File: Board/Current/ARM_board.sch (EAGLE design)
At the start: 171 parts, among them IC3 STM32F437VI, IC4 LM358DT, J1 USART/I2C, J10 ANALOG, J11 DGND, J12 DPWR, J13 DIGITAL, J14 SGND, J15 SPWR, J16 SERVO, J2 I2C2/USART3, J3 USART2, J5 SPI, J6 Bluesmirf, J7 SWD, J8 AGND, J9 APWR, Q1 STL4P2UH7, Q2 2STR1230, SW1 SW, U1 LSM330DLC, U10 BAV99, U11 BAV99, U12 USBLC6-2, U13 USBLC6-2, U14 STMPS2171MTR, U15 MC74HC164, U3 NC7SZU04, U4 L6206Q, U5 L6206Q, U6 SI7617, U7 SI7617, U8 SI7617, U9 SI7617, Y2 8MHz

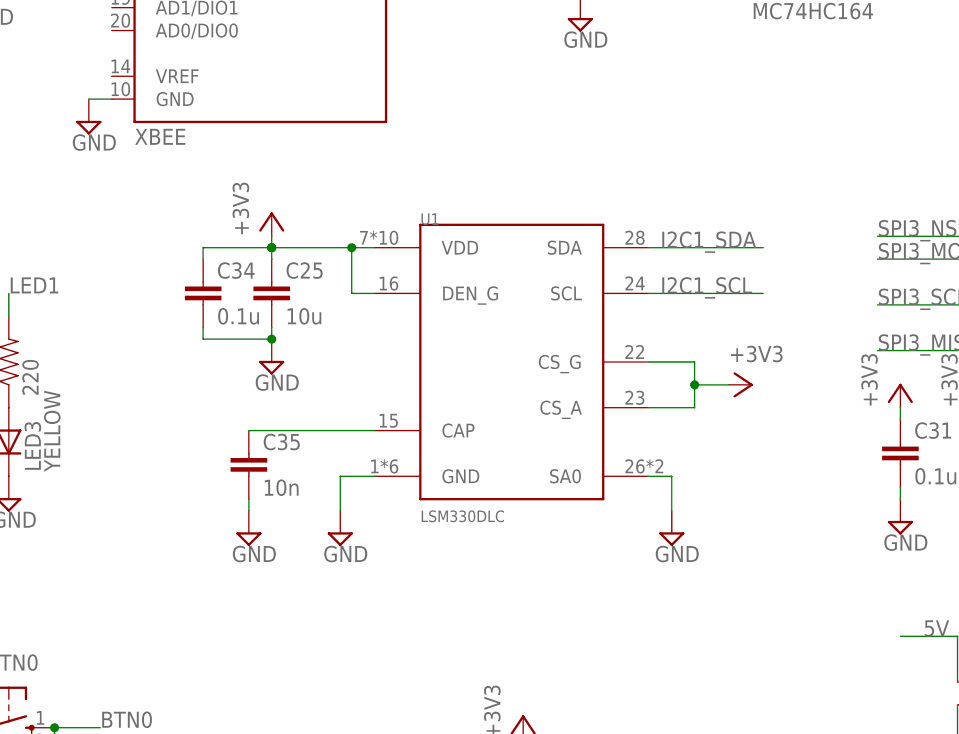
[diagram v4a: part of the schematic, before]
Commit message: Replaced LSM330DLC with LSM330 and re-added horse
LSM330 replaced LSM330DLC.
Re-added horse logo to board.
Moved labels in UART1 box down slightly.
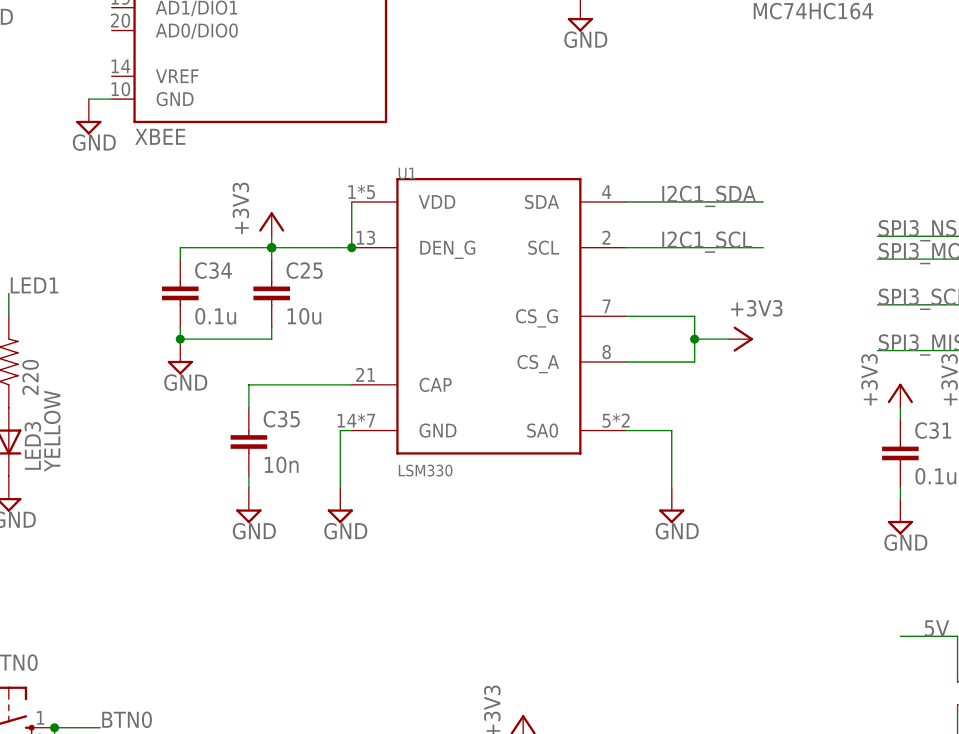
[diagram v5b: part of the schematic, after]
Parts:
- U1: value LSM330DLC -> LSM330; device r_cubed:LSM330DLC -> r_cubed:LSM330
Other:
- moved on the sheet: C34, C35, U1
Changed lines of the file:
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@@
 <setting verticaltext="up"/>
 </settings>
-<grid distance="0.05" unitdist="inch" unit="inch" style="lines" multiple="1" display="no" altdistance="0.01" altunitdist="inch" altunit="inch"/>
+<grid distance="0.1" unitdist="inch" unit="inch" style="lines" multiple="1" display="no" altdistance="0.01" altunitdist="inch" altunit="inch"/>
 <layers>
 <layer number="1" name="Top" color="4" fill="1" visible="no" active="no"/>
@@
 <part name="C43" library="SparkFun" deviceset="CAP" device="0402-CAP" value="0.1u"/>
 <part name="C44" library="SparkFun" deviceset="CAP_POL" device="D" value="680uF"/>
-<part name="U1" library="r_cubed" deviceset="LSM330DLC" device=""/>
+<part name="U1" library="r_cubed" deviceset="LSM330" device=""/>
 <part name="SUPPLY36" library="supply2" deviceset="GND" device=""/>
 <part name="SUPPLY55" library="supply2" deviceset="GND" device=""/>
@@
 <instance part="SUPPLY54" gate="GND" x="27.94" y="278.13"/>
 <instance part="C25" gate="G$1" x="271.78" y="82.55"/>
-<instance part="C34" gate="G$1" x="264.16" y="82.55"/>
-<instance part="C35" gate="G$1" x="269.24" y="63.5"/>
-<instance part="SUPPLY59" gate="GND" x="316.23" y="57.15"/>
-<instance part="SUPPLY61" gate="GND" x="271.78" y="76.2"/>
+<instance part="C34" gate="G$1" x="261.62" y="82.55"/>
+<instance part="C35" gate="G$1" x="269.24" y="66.04"/>
+<instance part="SUPPLY59" gate="GND" x="316.23" y="59.69"/>
+<instance part="SUPPLY61" gate="GND" x="261.62" y="76.2"/>
 <instance part="+3V2" gate="G$1" x="189.23" y="180.34" smashed="yes">
 <attribute name="VALUE" x="186.69" y="177.8" size="1.778" layer="96" rot="R90"/>
@@
 <instance part="C44" gate="G$1" x="228.6" y="237.49"/>
 <instance part="U1" gate="G$1" x="295.91" y="81.28"/>
-<instance part="SUPPLY36" gate="GND" x="279.4" y="57.15"/>
-<instance part="SUPPLY55" gate="GND" x="269.24" y="57.15"/>
-<instance part="+3V8" gate="G$1" x="325.12" y="73.66" smashed="yes" rot="R270">
-<attribute name="VALUE" x="322.58" y="76.2" size="1.778" layer="96"/>
+<instance part="SUPPLY36" gate="GND" x="279.4" y="59.69"/>
+<instance part="SUPPLY55" gate="GND" x="269.24" y="59.69"/>
+<instance part="+3V8" gate="G$1" x="325.12" y="78.74" smashed="yes" rot="R270">
+<attribute name="VALUE" x="322.58" y="81.28" size="1.778" layer="96"/>
 </instance>
 <instance part="U14" gate="G$1" x="304.8" y="222.25"/>
@@
 <pinref part="U1" gate="G$1" pin="GND"/>
 <pinref part="SUPPLY36" gate="GND" pin="GND"/>
-<wire x1="283.21" y1="63.5" x2="279.4" y2="63.5" width="0.1524" layer="91"/>
-<wire x1="279.4" y1="63.5" x2="279.4" y2="59.69" width="0.1524" layer="91"/>
+<wire x1="280.67" y1="68.58" x2="279.4" y2="68.58" width="0.1524" layer="91"/>
+<wire x1="279.4" y1="68.58" x2="279.4" y2="62.23" width="0.1524" layer="91"/>
 </segment>
 <segment>
 <pinref part="C34" gate="G$1" pin="2"/>
-<wire x1="264.16" y1="80.01" x2="264.16" y2="78.74" width="0.1524" layer="91"/>
+<wire x1="261.62" y1="80.01" x2="261.62" y2="78.74" width="0.1524" layer="91"/>
 <pinref part="SUPPLY61" gate="GND" pin="GND"/>
-<wire x1="264.16" y1="78.74" x2="271.78" y2="78.74" width="0.1524" layer="91"/>
 <pinref part="C25" gate="G$1" pin="2"/>
+<wire x1="261.62" y1="78.74" x2="271.78" y2="78.74" width="0.1524" layer="91"/>
 <wire x1="271.78" y1="78.74" x2="271.78" y2="80.01" width="0.1524" layer="91"/>
-<junction x="271.78" y="78.74"/>
+<junction x="261.62" y="78.74"/>
 </segment>
 <segment>
 <pinref part="C35" gate="G$1" pin="2"/>
 <pinref part="SUPPLY55" gate="GND" pin="GND"/>
-<wire x1="269.24" y1="60.96" x2="269.24" y2="59.69" width="0.1524" layer="91"/>
+<wire x1="269.24" y1="63.5" x2="269.24" y2="62.23" width="0.1524" layer="91"/>
 </segment>
 <segment>
 <pinref part="U1" gate="G$1" pin="SA0"/>
 <pinref part="SUPPLY59" gate="GND" pin="GND"/>
-<wire x1="313.69" y1="63.5" x2="316.23" y2="63.5" width="0.1524" layer="91"/>
-<wire x1="316.23" y1="63.5" x2="316.23" y2="59.69" width="0.1524" layer="91"/>
+<wire x1="311.15" y1="68.58" x2="316.23" y2="68.58" width="0.1524" layer="91"/>
+<wire x1="316.23" y1="68.58" x2="316.23" y2="62.23" width="0.1524" layer="91"/>
 </segment>
 <segment>
@@
 <segment>
 <pinref part="U1" gate="G$1" pin="SCL"/>
-<wire x1="313.69" y1="83.82" x2="326.39" y2="83.82" width="0.1524" layer="91"/>
-<label x="314.96" y="83.82" size="1.778" layer="95"/>
+<wire x1="311.15" y1="88.9" x2="326.39" y2="88.9" width="0.1524" layer="91"/>
+<label x="314.96" y="88.9" size="1.778" layer="95"/>
 </segment>
 <segment>
@@
 <segment>
 <pinref part="U1" gate="G$1" pin="SDA"/>
-<wire x1="313.69" y1="88.9" x2="326.39" y2="88.9" width="0.1524" layer="91"/>
-<label x="314.96" y="88.9" size="1.778" layer="95"/>
+<wire x1="311.15" y1="93.98" x2="326.39" y2="93.98" width="0.1524" layer="91"/>
+<label x="314.96" y="93.98" size="1.778" layer="95"/>
 </segment>
 <segment>
@@
 <segment>
 <pinref part="C34" gate="G$1" pin="1"/>
-<wire x1="264.16" y1="87.63" x2="264.16" y2="88.9" width="0.1524" layer="91"/>
+<wire x1="261.62" y1="87.63" x2="261.62" y2="88.9" width="0.1524" layer="91"/>
 <pinref part="+3V28" gate="G$1" pin="+3V3"/>
-<wire x1="264.16" y1="88.9" x2="271.78" y2="88.9" width="0.1524" layer="91"/>
+<wire x1="261.62" y1="88.9" x2="271.78" y2="88.9" width="0.1524" layer="91"/>
 <wire x1="271.78" y1="88.9" x2="271.78" y2="90.17" width="0.1524" layer="91"/>
 <pinref part="C25" gate="G$1" pin="1"/>
@@
 <wire x1="271.78" y1="88.9" x2="280.67" y2="88.9" width="0.1524" layer="91"/>
 <pinref part="U1" gate="G$1" pin="VDD"/>
-<wire x1="280.67" y1="88.9" x2="283.21" y2="88.9" width="0.1524" layer="91"/>
+<wire x1="280.67" y1="88.9" x2="280.67" y2="93.98" width="0.1524" layer="91"/>
 <junction x="271.78" y="88.9"/>
 <pinref part="U1" gate="G$1" pin="DEN_G"/>
-<wire x1="283.21" y1="83.82" x2="280.67" y2="83.82" width="0.1524" layer="91"/>
-<wire x1="280.67" y1="83.82" x2="280.67" y2="88.9" width="0.1524" layer="91"/>
 <junction x="280.67" y="88.9"/>
 </segment>
 <segment>
 <pinref part="U1" gate="G$1" pin="CS_A"/>
-<wire x1="313.69" y1="71.12" x2="318.77" y2="71.12" width="0.1524" layer="91"/>
-<wire x1="318.77" y1="71.12" x2="318.77" y2="73.66" width="0.1524" layer="91"/>
+<wire x1="311.15" y1="76.2" x2="318.77" y2="76.2" width="0.1524" layer="91"/>
+<wire x1="318.77" y1="76.2" x2="318.77" y2="78.74" width="0.1524" layer="91"/>
 <pinref part="U1" gate="G$1" pin="CS_G"/>
-<wire x1="318.77" y1="73.66" x2="318.77" y2="76.2" width="0.1524" layer="91"/>
-<wire x1="318.77" y1="76.2" x2="313.69" y2="76.2" width="0.1524" layer="91"/>
+<wire x1="318.77" y1="78.74" x2="318.77" y2="81.28" width="0.1524" layer="91"/>
+<wire x1="318.77" y1="81.28" x2="311.15" y2="81.28" width="0.1524" layer="91"/>
 <pinref part="+3V8" gate="G$1" pin="+3V3"/>
-<wire x1="322.58" y1="73.66" x2="318.77" y2="73.66" width="0.1524" layer="91"/>
-<junction x="318.77" y="73.66"/>
+<wire x1="322.58" y1="78.74" x2="318.77" y2="78.74" width="0.1524" layer="91"/>
+<junction x="318.77" y="78.74"/>
 </segment>
 <segment>
@@
 <pinref part="C35" gate="G$1" pin="1"/>
 <pinref part="U1" gate="G$1" pin="CAP"/>
-<wire x1="269.24" y1="68.58" x2="283.21" y2="68.58" width="0.1524" layer="91"/>
+<wire x1="269.24" y1="71.12" x2="269.24" y2="73.66" width="0.1524" layer="91"/>
+<wire x1="269.24" y1="73.66" x2="280.67" y2="73.66" width="0.1524" layer="91"/>
 </segment>
 </net>

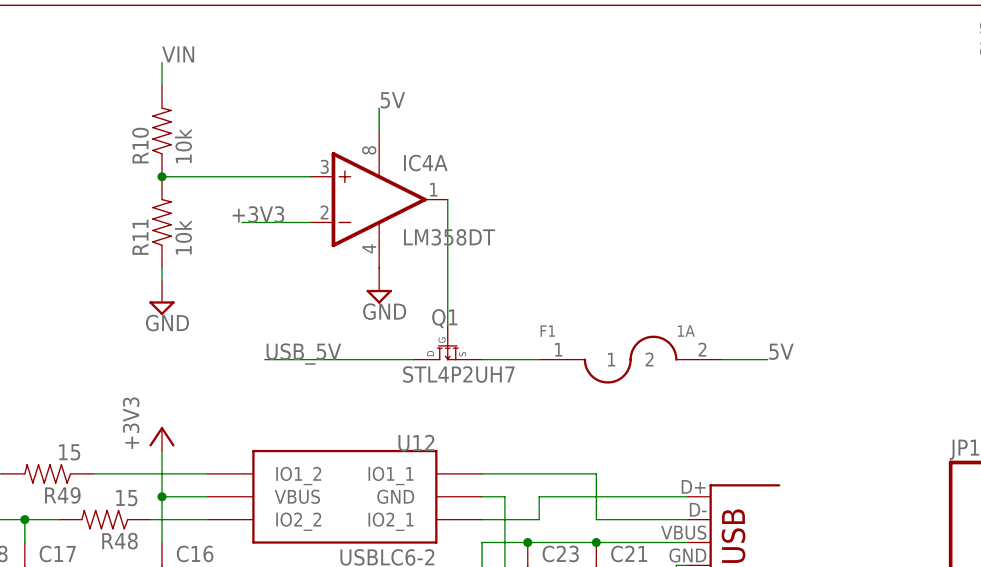
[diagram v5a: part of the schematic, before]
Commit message: Added 3.3V LDO for USB power to the schematic.
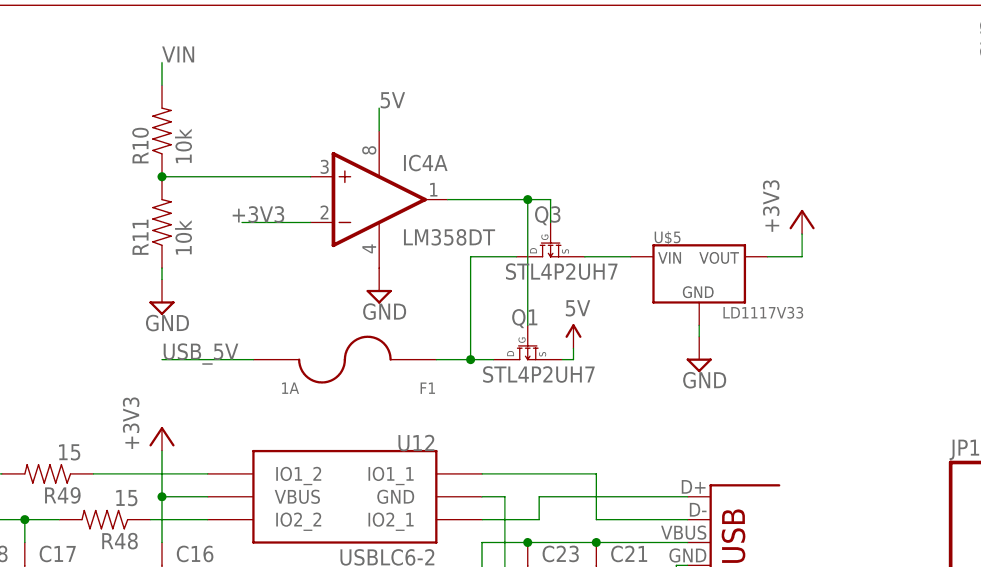
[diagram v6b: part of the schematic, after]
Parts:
- added Q3: STL4P2UH7, r_cubed:STL4P2UH7
- added U$5: LD1117V33, r_cubed:LD1117
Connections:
- new net N$22: Q3.S, U$5.VIN
- net +3V3: now also U$5.VOUT
- net 5V: now also Q1.S; no longer F1.2
- net GND: now also U$5.GND
- net N$14: now also Q3.G
- net N$15: now also Q1.D, Q3.D; no longer Q1.S
- net USB_5V: now also F1.2; no longer Q1.D
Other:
- moved on the sheet: Q1
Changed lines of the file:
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@@
 <setting verticaltext="up"/>
 </settings>
-<grid distance="0.1" unitdist="inch" unit="inch" style="lines" multiple="1" display="no" altdistance="0.01" altunitdist="inch" altunit="inch"/>
+<grid distance="0.05" unitdist="inch" unit="inch" style="lines" multiple="1" display="no" altdistance="0.01" altunitdist="inch" altunit="inch"/>
 <layers>
 <layer number="1" name="Top" color="4" fill="1" visible="no" active="no"/>
@@
 <part name="U$4" library="r_cubed" deviceset="DUAL-MOSFET" device=""/>
 <part name="+3V12" library="supply1" deviceset="+3V3" device=""/>
+<part name="U$5" library="r_cubed" deviceset="LD1117" device="" value="LD1117V33"/>
+<part name="Q3" library="r_cubed" deviceset="STL4P2UH7" device="" value="STL4P2UH7"/>
+<part name="U$6" library="SparkFun" deviceset="5V" device=""/>
+<part name="SUPPLY73" library="supply2" deviceset="GND" device=""/>
+<part name="+3V13" library="supply1" deviceset="+3V3" device=""/>
 </parts>
 <sheets>
@@
 <instance part="SUPPLY26" gate="GND" x="308.61" y="278.13"/>
 <instance part="R4" gate="G$1" x="224.79" y="196.85" rot="R90"/>
-<instance part="Q1" gate="G$1" x="316.23" y="271.78" smashed="yes" rot="R270">
-<attribute name="NAME" x="317.5" y="274.32" size="1.778" layer="95" rot="MR0"/>
-<attribute name="VALUE" x="323.85" y="267.97" size="1.778" layer="96" rot="MR0"/>
+<instance part="Q1" gate="G$1" x="325.12" y="271.78" smashed="yes" rot="R270">
+<attribute name="NAME" x="326.39" y="274.32" size="1.778" layer="95" rot="MR0"/>
+<attribute name="VALUE" x="332.74" y="267.97" size="1.778" layer="96" rot="MR0"/>
 </instance>
 <instance part="R10" gate="G$1" x="284.48" y="295.91" rot="R90"/>
@@
 </instance>
 <instance part="SUPPLY65" gate="GND" x="26.035" y="217.805"/>
-<instance part="F1" gate="G$1" x="336.55" y="270.51"/>
+<instance part="F1" gate="G$1" x="304.8" y="270.51" rot="R180"/>
 <instance part="JP2" gate="G$1" x="435.61" y="167.64" rot="R270"/>
 <instance part="+3V3" gate="G$1" x="424.18" y="215.9" smashed="yes">
@@
 <attribute name="VALUE" x="347.98" y="71.12" size="1.778" layer="96" rot="R90"/>
 </instance>
+<instance part="U$5" gate="G$1" x="344.17" y="279.4"/>
+<instance part="Q3" gate="G$1" x="327.66" y="283.21" smashed="yes" rot="R270">
+<attribute name="NAME" x="328.93" y="285.75" size="1.778" layer="95" rot="MR0"/>
+<attribute name="VALUE" x="335.28" y="279.4" size="1.778" layer="96" rot="MR0"/>
+</instance>
+<instance part="U$6" gate="G$1" x="330.2" y="271.78"/>
+<instance part="SUPPLY73" gate="GND" x="344.17" y="270.51"/>
+<instance part="+3V13" gate="G$1" x="355.6" y="287.02" smashed="yes">
+<attribute name="VALUE" x="353.06" y="284.48" size="1.778" layer="96" rot="R90"/>
+</instance>
 </instances>
 <busses>
@@
 <wire x1="39.37" y1="267.97" x2="39.37" y2="266.7" width="0.1524" layer="91"/>
 </segment>
+<segment>
+<pinref part="U$5" gate="G$1" pin="GND"/>
+<wire x1="344.17" y1="274.32" x2="344.17" y2="273.05" width="0.1524" layer="91"/>
+<pinref part="SUPPLY73" gate="GND" pin="GND"/>
+</segment>
 </net>
 <net name="5V" class="0">
@@
 </segment>
 <segment>
-<pinref part="F1" gate="G$1" pin="2"/>
-<wire x1="346.71" y1="270.51" x2="351.79" y2="270.51" width="0.1524" layer="91"/>
-<label x="351.79" y="270.51" size="1.778" layer="95"/>
-</segment>
-<segment>
 <pinref part="SG1" gate="G$1" pin="1"/>
 <wire x1="347.98" y1="40.64" x2="347.98" y2="45.72" width="0.1524" layer="91"/>
@@
 <junction x="219.71" y="278.13"/>
 </segment>
+<segment>
+<pinref part="Q1" gate="G$1" pin="S"/>
+<pinref part="U$6" gate="G$1" pin="5V"/>
+<wire x1="328.93" y1="270.51" x2="330.2" y2="270.51" width="0.1524" layer="91"/>
+<wire x1="330.2" y1="270.51" x2="330.2" y2="271.78" width="0.1524" layer="91"/>
+</segment>
 </net>
 <net name="VIN" class="0">
@@
 <segment>
 <pinref part="IC4" gate="A" pin="OUT"/>
-<wire x1="316.23" y1="288.29" x2="316.23" y2="274.32" width="0.1524" layer="91"/>
+<wire x1="316.23" y1="288.29" x2="325.12" y2="288.29" width="0.1524" layer="91"/>
+<wire x1="325.12" y1="288.29" x2="325.12" y2="274.32" width="0.1524" layer="91"/>
 <pinref part="Q1" gate="G$1" pin="G"/>
+<pinref part="Q3" gate="G$1" pin="G"/>
+<wire x1="327.66" y1="285.75" x2="327.66" y2="288.29" width="0.1524" layer="91"/>
+<wire x1="327.66" y1="288.29" x2="325.12" y2="288.29" width="0.1524" layer="91"/>
+<junction x="325.12" y="288.29"/>
 </segment>
 </net>
@@
 </segment>
 <segment>
-<pinref part="Q1" gate="G$1" pin="D"/>
-<wire x1="312.42" y1="270.51" x2="295.91" y2="270.51" width="0.1524" layer="91"/>
-<label x="295.91" y="270.51" size="1.778" layer="95"/>
-</segment>
-<segment>
 <pinref part="IC3" gate="PORTA_H" pin="PA9"/>
 <wire x1="151.13" y1="123.19" x2="148.59" y2="123.19" width="0.1524" layer="91"/>
 <label x="139.7" y="123.19" size="1.778" layer="95"/>
 </segment>
+<segment>
+<pinref part="F1" gate="G$1" pin="2"/>
+<wire x1="294.64" y1="270.51" x2="284.48" y2="270.51" width="0.1524" layer="91"/>
+<label x="284.48" y="270.51" size="1.778" layer="95"/>
+</segment>
 </net>
 <net name="LCD_RS" class="0">
@@
 <wire x1="350.52" y1="71.12" x2="350.52" y2="67.31" width="0.1524" layer="91"/>
 </segment>
+<segment>
+<pinref part="U$5" gate="G$1" pin="VOUT"/>
+<wire x1="351.79" y1="281.94" x2="355.6" y2="281.94" width="0.1524" layer="91"/>
+<wire x1="355.6" y1="281.94" x2="355.6" y2="284.48" width="0.1524" layer="91"/>
+<pinref part="+3V13" gate="G$1" pin="+3V3"/>
+</segment>
 </net>
 <net name="N$47" class="0">
@@
 </segment>
 </net>
-<net name="N$15" class="0">
-<segment>
-<pinref part="Q1" gate="G$1" pin="S"/>
-<pinref part="F1" gate="G$1" pin="1"/>
-<wire x1="320.04" y1="270.51" x2="326.39" y2="270.51" width="0.1524" layer="91"/>
-</segment>
-</net>
 <net name="ANALOG3" class="0">
 <segment>
@@
 </segment>
 </net>
+<net name="N$15" class="0">
+<segment>
+<pinref part="F1" gate="G$1" pin="1"/>
+<pinref part="Q1" gate="G$1" pin="D"/>
+<wire x1="314.96" y1="270.51" x2="318.77" y2="270.51" width="0.1524" layer="91"/>
+<wire x1="318.77" y1="270.51" x2="321.31" y2="270.51" width="0.1524" layer="91"/>
+<pinref part="Q3" gate="G$1" pin="D"/>
+<wire x1="323.85" y1="281.94" x2="318.77" y2="281.94" width="0.1524" layer="91"/>
+<wire x1="318.77" y1="281.94" x2="318.77" y2="270.51" width="0.1524" layer="91"/>
+<junction x="318.77" y="270.51"/>
+</segment>
+</net>
+<net name="N$22" class="0">
+<segment>
+<pinref part="Q3" gate="G$1" pin="S"/>
+<pinref part="U$5" gate="G$1" pin="VIN"/>
+<wire x1="331.47" y1="281.94" x2="336.55" y2="281.94" width="0.1524" layer="91"/>
+</segment>
+</net>
